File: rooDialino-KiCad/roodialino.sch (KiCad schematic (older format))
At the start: 47 parts, among them J2 ICSP, J3 FTDI, SW1 SW_Push, U3 ATmega328P, Y1 16MHz

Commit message: More schematics
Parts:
- removed Q? (x2): 2N7002, Package_TO_SOT_SMD:SOT-23, symbol Transistor_FET:2N7002
- removed R? (x2): 10k, Resistor_SMD:R_0805_2012Metric, symbol Device:R
- removed SW1: SW_Push, Button_Switch_THT:SW_PUSH_6mm_H7.3mm, symbol Switch:SW_Push
- removed TP11: >>, TestPoint:TestPoint_THTPad_D1.5mm_Drill0.7mm, symbol Connector:TestPoint
- added C? (x2): 100n, Capacitor_SMD:C_0805_2012Metric, symbol Device:C_Small
- added Q? (x2): 2N7002, Package_TO_SOT_SMD:SOT-23, symbol Transistor_FET:2N7002
- added R? (x5): 10k, Resistor_SMD:R_0805_2012Metric, symbol Device:R
- added TP?: A0, TestPoint:TestPoint_THTPad_D1.5mm_Drill0.7mm, symbol Connector:TestPoint
- added TP?: GPIO5, TestPoint:TestPoint_THTPad_D1.5mm_Drill0.7mm, symbol Connector:TestPoint
- added TP?: GPIO6, TestPoint:TestPoint_THTPad_D1.5mm_Drill0.7mm, symbol Connector:TestPoint
- added TP?: SDA, TestPoint:TestPoint_THTPad_D1.5mm_Drill0.7mm, symbol Connector:TestPoint
- added TP?: SCL, TestPoint:TestPoint_THTPad_D1.5mm_Drill0.7mm, symbol Connector:TestPoint
- added TP?: IRTX, TestPoint:TestPoint_THTPad_D1.5mm_Drill0.7mm, symbol Connector:TestPoint
- added TP?: IRRCV, TestPoint:TestPoint_THTPad_D1.5mm_Drill0.7mm, symbol Connector:TestPoint
- added TP?: GND, TestPoint:TestPoint_THTPad_D1.5mm_Drill0.7mm, symbol Connector:TestPoint
- added TP?: +3.3V, TestPoint:TestPoint_THTPad_D1.5mm_Drill0.7mm, symbol Connector:TestPoint
- added TP?: +5V, TestPoint:TestPoint_THTPad_D1.5mm_Drill0.7mm, symbol Connector:TestPoint
- added U?: TXS0108EPW, Package_SO:TSSOP-20_4.4x6.5mm_P0.65mm, symbol Logic_LevelTranslator:TXS0108EPW
- R? (x5): value 330 -> 470
- TP15: value D10 -> D9
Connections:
- net < is gone; now on net LEDRON: U3.24 (PC1)
- net >> is gone; now on net IRRCV: U3.11 (PD7)
- net IR is gone; now on net IRTX: R?.1, R?.1
- net LEDP is gone; now on net LEDVOL-: U3.9 (PD5)
- net SSR is gone; now on net LEDVOL+: U3.10 (PD6)
- net VOL+ is gone; now on net +3V3: J?.17 (Pin_17)
- net o is gone; now on net LEDROFF: U3.25 (PC2)
- net ~STOP~ is gone; now on net D9: U3.13 (PB1)
- net +5V: now also C?.1, R?.2, R?.2, TP?.1, U?.19 (VCCB)
- net BTTN: now also C?.2, R?.2
- net GNDD: now also C?.2, C?.2, R?.1, TP?.1, U?.11 (GND)
- net IRRCV: now also TP?.1
- net MISO: no longer J?.18 (Pin_18), U3.16 (PB4)
- net MOSI: no longer J?.23 (Pin_23), U3.15 (PB3)
- net RX: no longer U3.30 (PD0)
- net SCK: no longer J?.24 (Pin_24), U3.17 (PB5)
- net SCL: now also TP?.1
- net SDA: now also TP?.1
- net TX: no longer U3.31 (PD1)
- net ~RST~: now also U?.12 (B8)
- net +3V3: now reaches J?.1 (Pin_1)
- net +3V3: now also C?.1, Q?.1 (G), Q?.1 (G), R?.2, R?.2, R?.2, TP?.1, U?.10 (OE), U?.2 (VCCA)
- net RX3: now reaches J?.10 (Pin_10)
- net RX3: now also U?.4 (A3)
- net VOL+3: now reaches J?.11 (Pin_11)
- net VOL+3: now also U?.1 (A1)
- net MISO3: now reaches J?.12 (Pin_12)
- net MISO3: now also U?.6 (A5)
- net VOL-3: now reaches J?.13 (Pin_13)
- net VOL-3: now also U?.3 (A2)
- net MOSI3: now reaches J?.16 (Pin_16)
- net MOSI3: now also U?.7 (A6)
- net GPIO5: now reaches J?.29 (Pin_29)
- net GPIO5: now also Q?.2 (S), R?.1, TP?.1
- net GPIO6: now reaches J?.31 (Pin_31)
- net GPIO6: now also Q?.2 (S), R?.1, TP?.1
- net RST3: now reaches J?.32 (Pin_32)
- net RST3: now also U?.9 (A8)
- net TX3: now reaches J?.8 (Pin_8)
- net TX3: now also U?.5 (A4)
- net 1 renamed LEDRON
- net 2 renamed LEDROFF
- net 3 renamed LEDRSTATE
- net LEDRSTATE: now also U3.14 (PB2)
- net 4 renamed LEDVOL-
- net 5 renamed LEDVOL+
- net << renamed A0
- net A0: now also Q?.3 (D), R?.1, TP?.1
- net >: no longer names the net of U3.26 (PC3)
- net D10 renamed D9
- net D9: now also Q?.3 (D), R?.1; no longer U3.14 (PB2)
- net ICP1 renamed IRTX
- net IRTX: now also TP?.1
- net INT0 renamed VOL+5
- net VOL+5: now also U?.20 (B1)
- net INT1 renamed VOL-5
- net VOL-5: now also U?.18 (B2)
- net VOL-: no longer names the net of J?.27 (Pin_27)
- new net MISO5: U3.16 (PB4), U?.15 (B5)
- new net MOSI5: U3.15 (PB3), U?.14 (B6)
- new net RX5: U3.30 (PD0), U?.16 (B4)
- new net SCK3: J?.18 (Pin_18), U?.8 (A7)
- new net SCK5: U3.17 (PB5), U?.13 (B7)
- new net TX5: U3.31 (PD1), U?.17 (B3)
- no-connect marks 2 -> 23
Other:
- moved on the sheet: C?, D?, J2, J?, R?, TP15

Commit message: Footprints completed
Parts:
- added C12: 100u, Capacitor_SMD:C_1206_3216Metric, symbol Device:C_Small
- C1: footprint Capacitor_SMD:C_0805_2012Metric -> Capacitor_SMD:C_0603_1608Metric; LCSC (none) -> C14663
- C10: renamed from C?; footprint Capacitor_SMD:C_0805_2012Metric -> Capacitor_SMD:C_0603_1608Metric
- C11, C3, C8, C9: renamed from C?; footprint Capacitor_SMD:C_0805_2012Metric -> Capacitor_SMD:C_0603_1608Metric; LCSC (none) -> C14663
- C2, C7: renamed from C?; footprint (none) -> Capacitor_SMD:C_1210_3225Metric; LCSC (none) -> C16133
- C4: renamed from C8; footprint Capacitor_SMD:C_0805_2012Metric -> Capacitor_SMD:C_0402_1005Metric; LCSC (none) -> C1555
- C5: renamed from C9; footprint Capacitor_SMD:C_0805_2012Metric -> Capacitor_SMD:C_0402_1005Metric; LCSC (none) -> C1555
- C6: renamed from C13; footprint Capacitor_SMD:C_0805_2012Metric -> Capacitor_SMD:C_0603_1608Metric; LCSC (none) -> C14663
- D1, D2, D3: renamed from D?; footprint (none) -> LED_SMD:LED_0603_1608Metric; LCSC (none) -> C72041
- D4: renamed from D?; footprint (none) -> LED_SMD:LED_0805_2012Metric; LCSC (none) -> C84256
- D5: renamed from D?; footprint (none) -> LED_SMD:LED_0805_2012Metric; LCSC (none) -> C2297
- D6, D8: renamed from D?; footprint (none) -> LED_THT:LED_D5.0mm_Horizontal_O1.27mm_Z3.0mm_IRBlack
- D7: renamed from D?; footprint (none) -> LED_THT:LED_D5.0mm_Clear
- J1: renamed from J?; footprint (none) -> Connector_PinSocket_2.54mm:PinSocket_2x20_P2.54mm_Vertical
- J4: renamed from J?; footprint (none) -> Connector_PinHeader_2.54mm:PinHeader_1x03_P2.54mm_Vertical
- J5: renamed from J?; footprint (none) -> Connector_PinHeader_2.54mm:PinHeader_1x02_P2.54mm_Vertical
- Q1, Q2, Q3: renamed from Q?; LCSC (none) -> C8545
- R1: renamed from R9; footprint Resistor_SMD:R_0805_2012Metric -> Resistor_SMD:R_0402_1005Metric; LCSC (none) -> C25879
- R10, R4, R5, R6, R7: renamed from R?; LCSC (none) -> C17710
- R11, R9: renamed from R?; footprint Resistor_SMD:R_0805_2012Metric -> Resistor_SMD:R_0402_1005Metric
- R12, R14, R15, R16, R17, R18: renamed from R?; footprint Resistor_SMD:R_0805_2012Metric -> Resistor_SMD:R_0402_1005Metric; LCSC (none) -> C25744
- R13: renamed from R?; LCSC (none) -> C17634
- R2: renamed from R10; footprint Resistor_SMD:R_0805_2012Metric -> Resistor_SMD:R_0402_1005Metric; LCSC (none) -> C25879
- R3: renamed from R11; footprint Resistor_SMD:R_0805_2012Metric -> Resistor_SMD:R_0402_1005Metric; LCSC (none) -> C25744
- R8: renamed from R?; value 8R2 -> 5R1; LCSC (none) -> C17724
- SW1: renamed from SW?; footprint Button_Switch_THT:SW_PUSH_6mm_H7.3mm -> Button_Switch_SMD:SW_SPST_TL3342; LCSC (none) -> C318884
- U1: renamed from U3; LCSC (none) -> C14877
- U2: renamed from U?; footprint OptoDevice:Vishay_CAST-3Pin -> OptoDevice:Vishay_MINICAST-3Pin
- U3: renamed from U?; LCSC (none) -> C17206
- Y1: footprint Crystal:Crystal_SMD_Abracon_ABM3-2Pin_5.0x3.2mm -> Crystal:Crystal_SMD_3225-4Pin_3.2x2.5mm; LCSC (none) -> C13738
- gave numbers to parts that had none: 10
- renumbered TP15 to TP1
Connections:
- net 5V is gone; now on net +5V: J3.3 (Pin_3)
- net MISO is gone; now on net MISO5: J2.1 (MISO)
- net MOSI is gone; now on net MOSI5: J2.4 (MOSI)
- net RX is gone; now on net RX5: J3.4 (Pin_4)
- net SCK is gone; now on net SCK5: J2.3 (SCK)
- net TX is gone; now on net TX5: J3.5 (Pin_5)
- net +5V: now also C12.1
- net GNDD: now also C12.2
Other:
- moved on the sheet: C10, C11, C6, C9, D1, D2, D3, D4, D5, J2, J3, R10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

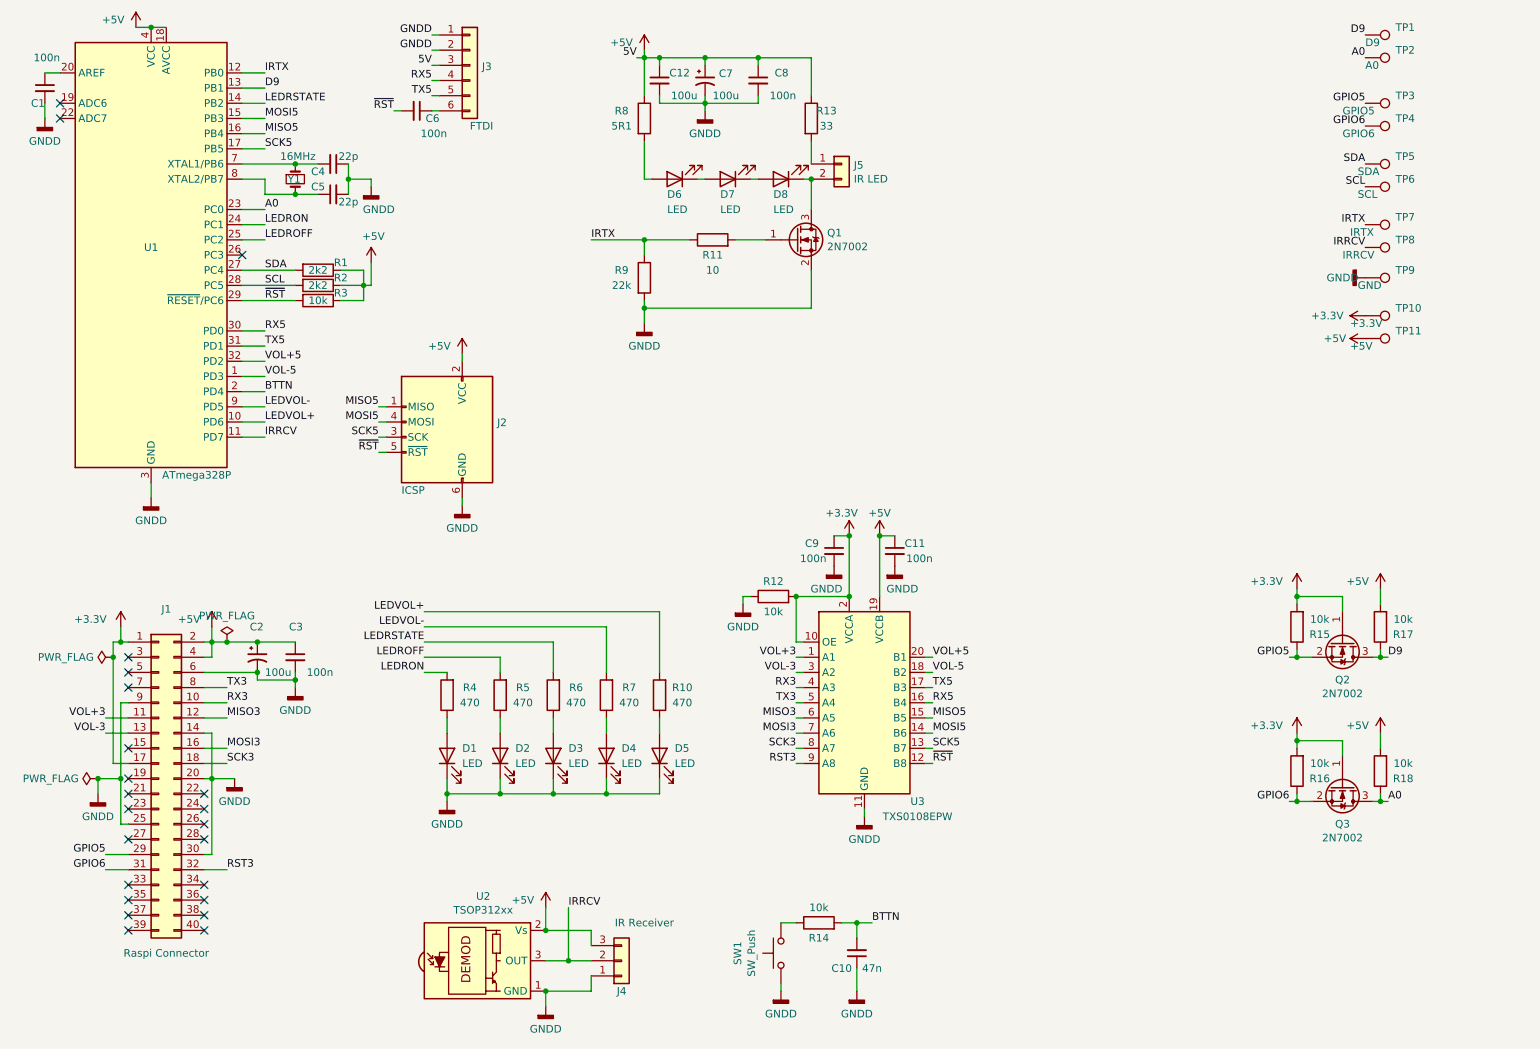
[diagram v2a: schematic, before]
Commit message: all parts placed on board
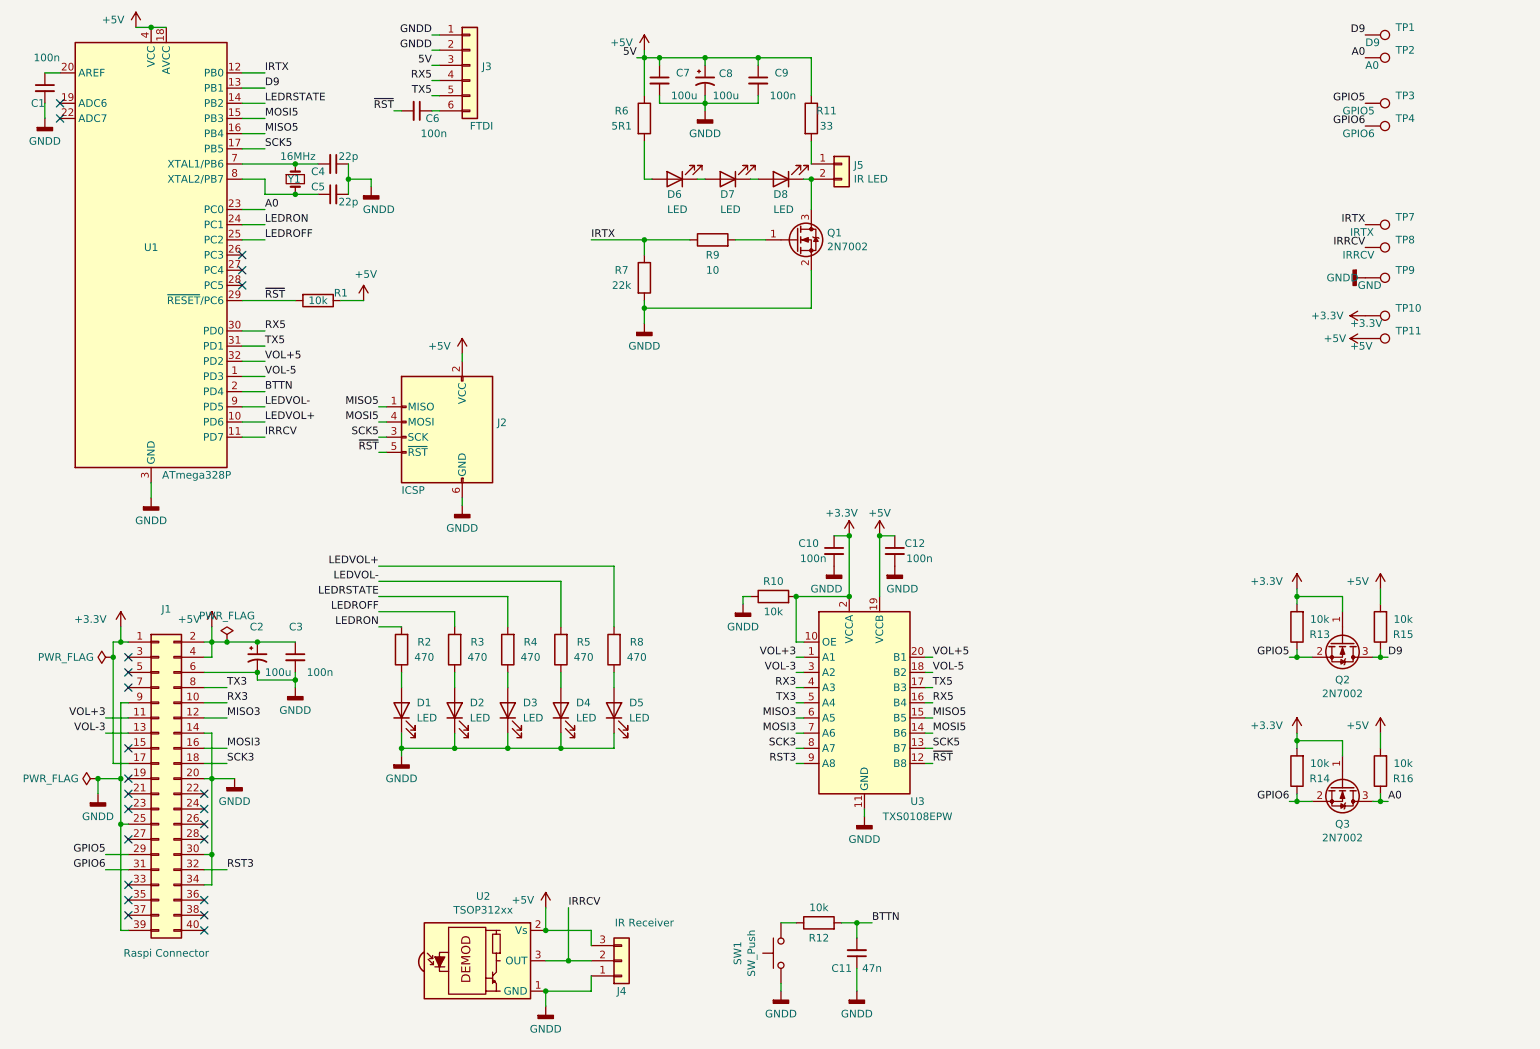
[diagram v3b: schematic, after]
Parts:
- removed R1, R2: 2k2, Resistor_SMD:R_0402_1005Metric, symbol Device:R
- removed TP5: SDA, TestPoint:TestPoint_THTPad_D1.5mm_Drill0.7mm, symbol Connector:TestPoint
- removed TP6: SCL, TestPoint:TestPoint_THTPad_D1.5mm_Drill0.7mm, symbol Connector:TestPoint
- J3: footprint Connector_PinHeader_2.54mm:PinHeader_1x06_P2.54mm_Horizontal -> Connector_PinHeader_2.54mm:PinHeader_1x06_P2.54mm_Vertical
- renumbered C9 to C10, C10 to C11, C11 to C12, C12 to C7, C7 to C8, C8 to C9, R3 to R1, R12 to R10, R13 to R11, R14 to R12, R15 to R13, R16 to R14, R17 to R15, R18 to R16, R4 to R2, R5 to R3, R6 to R4, R7 to R5, R8 to R6, R9 to R7, R10 to R8, R11 to R9
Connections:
- net GNDD: now also J1.34 (Pin_34), J1.39 (Pin_39)
- net SCL: no longer names the net of U1.28 (PC5)
- net SDA: no longer names the net of U1.27 (PC4)
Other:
- moved on the sheet: D1, D2, D3, D4, D5, R2, R3, R4, R5, R8

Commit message: More routing
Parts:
- renumbered R8 to R6, R6 to R7, R7 to R8, TP7 to TP5, TP8 to TP6, TP9 to TP7, TP10 to TP8, TP11 to TP9
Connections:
- net MOSI3: now also U3.4 (A3); no longer U3.7 (A6)
- net MOSI5: now also U3.17 (B3); no longer U3.14 (B6)
- net RST3: now also U3.1 (A1); no longer U3.9 (A8)
- net RX3: now also U3.8 (A7); no longer U3.4 (A3)
- net RX5: now also U3.13 (B7); no longer U3.16 (B4)
- net SCK3: now also U3.3 (A2); no longer U3.8 (A7)
- net SCK5: now also U3.18 (B2); no longer U3.13 (B7)
- net TX3: now also U3.9 (A8); no longer U3.5 (A4)
- net TX5: now also U3.12 (B8); no longer U3.17 (B3)
- net VOL+3: now also U3.7 (A6); no longer U3.1 (A1)
- net VOL+5: now also U3.14 (B6); no longer U3.20 (B1)
- net VOL-3: now also U3.5 (A4); no longer U3.3 (A2)
- net VOL-5: now also U3.16 (B4); no longer U3.18 (B2)
- net ~RST~: now also U3.20 (B1); no longer U3.12 (B8)
- net at C4.2, U1.7 (XTAL1/PB6): now also Y1.2; no longer Y1.1
- net at C5.1, U1.8 (XTAL2/PB7): now also Y1.1; no longer Y1.2
- no-connect marks 23 -> 24
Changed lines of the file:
@@
 P 2350 1800
 F 0 "Y1" V 2350 1750 50  0000 L CNN
-F 1 "16MHz" V 2200 1700 50  0000 L CNN
+F 1 "16MHz" V 2500 1700 50  0000 L CNN
 F 2 "Crystal:Crystal_SMD_3225-4Pin_3.2x2.5mm" H 2350 1800 50  0001 C CNN
 F 3 "~" H 2350 1800 50  0001 C CNN
 F 4 "C13738" V 2350 1800 50  0001 C CNN "LCSC"
 	1    2350 1800
-	0    1    1    0
+	0    1    -1   0
 $EndComp
 Wire Wire Line
@@
 $EndComp
 $Comp
-L Device:R R8
+L Device:R R6
 U 1 1 616F1CC8
 P 4450 4900
-F 0 "R8" H 4300 4850 50  0000 C CNN
+F 0 "R6" H 4300 4850 50  0000 C CNN
 F 1 "470" H 4300 4950 50  0000 C CNN
 F 2 "Resistor_SMD:R_0805_2012Metric" V 4380 4900 50  0001 C CNN
@@
 $EndComp
 $Comp
-L Device:R R7
+L Device:R R8
 U 1 1 6178C156
 P 4650 2450
-F 0 "R7" H 4500 2500 50  0000 C CNN
+F 0 "R8" H 4500 2500 50  0000 C CNN
 F 1 "22k" H 4500 2400 50  0000 C CNN
 F 2 "Resistor_SMD:R_0402_1005Metric" V 4580 2450 50  0001 C CNN
@@
 $EndComp
 $Comp
-L Device:R R6
+L Device:R R7
 U 1 1 617E0549
 P 4650 1400
-F 0 "R6" H 4500 1450 50  0000 C CNN
+F 0 "R7" H 4500 1450 50  0000 C CNN
 F 1 "5R1" H 4500 1350 50  0000 C CNN
 F 2 "Resistor_SMD:R_0805_2012Metric" V 4580 1400 50  0001 C CNN
@@
 	9500 5900 9550 5900
 Connection ~ 9500 5900
-Text Label 5650 5050 2    50   ~ 0
+Text Label 5650 5250 2    50   ~ 0
 VOL-3
-Text Label 5650 5150 2    50   ~ 0
+Text Label 5650 5550 2    50   ~ 0
 RX3
-Text Label 5650 5250 2    50   ~ 0
+Text Label 5650 5650 2    50   ~ 0
 TX3
 Text Label 8900 4950 2    50   ~ 0
@@
 Text Label 9550 5900 0    50   ~ 0
 A0
+Text Label 6550 5550 0    50   ~ 0
+RX5
+Text Label 6550 5650 0    50   ~ 0
+TX5
 Text Label 6550 5250 0    50   ~ 0
-RX5
-Text Label 6550 5150 0    50   ~ 0
-TX5
-Text Label 6550 5050 0    50   ~ 0
 VOL-5
-Text Label 6550 4950 0    50   ~ 0
+Text Label 6550 5450 0    50   ~ 0
 VOL+5
 $Comp
-L Connector:TestPoint TP7
+L Connector:TestPoint TP5
 U 1 1 61EBC057
 P 9400 2100
-F 0 "TP7" V 9350 2300 50  0000 L CNN
+F 0 "TP5" V 9350 2300 50  0000 L CNN
 F 1 "IRTX" V 9450 2000 50  0000 L CNN
 F 2 "TestPoint:TestPoint_THTPad_D1.5mm_Drill0.7mm" H 9600 2100 50  0001 C CNN
@@
 $EndComp
 $Comp
-L Connector:TestPoint TP8
+L Connector:TestPoint TP6
 U 1 1 61EBC300
 P 9400 2250
-F 0 "TP8" V 9350 2450 50  0000 L CNN
+F 0 "TP6" V 9350 2450 50  0000 L CNN
 F 1 "IRRCV" V 9450 2100 50  0000 L CNN
 F 2 "TestPoint:TestPoint_THTPad_D1.5mm_Drill0.7mm" H 9600 2250 50  0001 C CNN
@@
 IRRCV
 $Comp
-L Connector:TestPoint TP9
+L Connector:TestPoint TP7
 U 1 1 61EBCD0A
 P 9400 2450
-F 0 "TP9" V 9350 2650 50  0000 L CNN
+F 0 "TP7" V 9350 2650 50  0000 L CNN
 F 1 "GND" V 9450 2400 50  0000 L CNN
 F 2 "TestPoint:TestPoint_THTPad_D1.5mm_Drill0.7mm" H 9600 2450 50  0001 C CNN
@@
 	1    0    0    -1
 $EndComp
-Text Label 5650 4950 2    50   ~ 0
+Text Label 5650 5450 2    50   ~ 0
 VOL+3
 Text Label 5650 5350 2    50   ~ 0
 MISO3
-Text Label 5650 5450 2    50   ~ 0
+Text Label 5650 5150 2    50   ~ 0
 MOSI3
-Text Label 5650 5550 2    50   ~ 0
+Text Label 5650 5050 2    50   ~ 0
 SCK3
-Text Label 5650 5650 2    50   ~ 0
+Text Label 5650 4950 2    50   ~ 0
 RST3
-Text Label 6550 5650 0    50   ~ 0
+Text Label 6550 4950 0    50   ~ 0
 ~RST~
-Text Label 6550 5550 0    50   ~ 0
+Text Label 6550 5050 0    50   ~ 0
 SCK5
-Text Label 6550 5450 0    50   ~ 0
+Text Label 6550 5150 0    50   ~ 0
 MOSI5
 Text Label 6550 5350 0    50   ~ 0
@@
 	6100 5950 6100 6000
 $Comp
-L Connector:TestPoint TP10
+L Connector:TestPoint TP8
 U 1 1 61FF236E
 P 9400 2700
-F 0 "TP10" V 9350 2900 50  0000 L CNN
+F 0 "TP8" V 9350 2900 50  0000 L CNN
 F 1 "+3.3V" V 9450 2600 50  0000 L CNN
 F 2 "TestPoint:TestPoint_THTPad_D1.5mm_Drill0.7mm" H 9600 2700 50  0001 C CNN
@@
 $EndComp
 $Comp
-L Connector:TestPoint TP11
+L Connector:TestPoint TP9
 U 1 1 61FF42DA
 P 9400 2850
-F 0 "TP11" V 9350 3050 50  0000 L CNN
+F 0 "TP9" V 9350 3050 50  0000 L CNN
 F 1 "+5V" V 9450 2750 50  0000 L CNN
 F 2 "TestPoint:TestPoint_THTPad_D1.5mm_Drill0.7mm" H 9600 2850 50  0001 C CNN
@@
 NoConn ~ 2000 2400
 NoConn ~ 2000 2500
+NoConn ~ 2600 2700
 $EndSCHEMATC
